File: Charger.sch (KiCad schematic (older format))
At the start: 2 parts

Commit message: added ckt
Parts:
- removed R? (x2): R, symbol Device:R
- added C? (x3): CAP, symbol pspice:CAP
- added D? (x4): 1N914, Diode_THT:D_DO-35_SOD27_P7.62mm_Horizontal, symbol Diode:1N914
- added D?: BZX84Cxx, Diode_SMD:D_SOT-23_ANK, symbol Diode:BZX84Cxx
- added R? (x2): R, symbol Device:R
- added U?: LT1085-5.0, symbol Regulator_Linear:LT1085-5.0
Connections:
- net labels added: AC, GND
- wire segments 0 -> 35
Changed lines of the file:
@@
 $EndDescr
 $Comp
+L Diode:1N914 D?
+U 1 1 6031057C
+P 3100 2550
+F 0 "D?" V 3054 2630 50  0000 L CNN
+F 1 "1N914" V 3145 2630 50  0000 L CNN
+F 2 "Diode_THT:D_DO-35_SOD27_P7.62mm_Horizontal" H 3100 2375 50  0001 C CNN
+F 3 "http://www.vishay.com/docs/85622/1n914.pdf" H 3100 2550 50  0001 C CNN
+	1    3100 2550
+	0    1    1    0
+$EndComp
+$Comp
+L Diode:1N914 D?
+U 1 1 60311C82
+P 3100 3800
+F 0 "D?" V 3054 3880 50  0000 L CNN
+F 1 "1N914" V 3145 3880 50  0000 L CNN
+F 2 "Diode_THT:D_DO-35_SOD27_P7.62mm_Horizontal" H 3100 3625 50  0001 C CNN
+F 3 "http://www.vishay.com/docs/85622/1n914.pdf" H 3100 3800 50  0001 C CNN
+	1    3100 3800
+	0    1    1    0
+$EndComp
+$Comp
+L Diode:1N914 D?
+U 1 1 60312AAD
+P 4200 2550
+F 0 "D?" V 4154 2630 50  0000 L CNN
+F 1 "1N914" V 4245 2630 50  0000 L CNN
+F 2 "Diode_THT:D_DO-35_SOD27_P7.62mm_Horizontal" H 4200 2375 50  0001 C CNN
+F 3 "http://www.vishay.com/docs/85622/1n914.pdf" H 4200 2550 50  0001 C CNN
+	1    4200 2550
+	0    1    1    0
+$EndComp
+$Comp
+L Diode:1N914 D?
+U 1 1 60313CDB
+P 4200 3800
+F 0 "D?" V 4154 3880 50  0000 L CNN
+F 1 "1N914" V 4245 3880 50  0000 L CNN
+F 2 "Diode_THT:D_DO-35_SOD27_P7.62mm_Horizontal" H 4200 3625 50  0001 C CNN
+F 3 "http://www.vishay.com/docs/85622/1n914.pdf" H 4200 3800 50  0001 C CNN
+	1    4200 3800
+	0    1    1    0
+$EndComp
+$Comp
+L pspice:CAP C?
+U 1 1 60316869
+P 5050 3250
+F 0 "C?" H 5228 3296 50  0000 L CNN
+F 1 "CAP" H 5228 3205 50  0000 L CNN
+F 2 "" H 5050 3250 50  0001 C CNN
+F 3 "~" H 5050 3250 50  0001 C CNN
+	1    5050 3250
+	1    0    0    -1
+$EndComp
+$Comp
+L Diode:BZX84Cxx D?
+U 1 1 603170B0
+P 6000 3550
+F 0 "D?" V 5954 3630 50  0000 L CNN
+F 1 "BZX84Cxx" V 6045 3630 50  0000 L CNN
+F 2 "Diode_SMD:D_SOT-23_ANK" H 6000 3375 50  0001 C CNN
+F 3 "https://diotec.com/tl_files/diotec/files/pdf/datasheets/bzx84c2v4.pdf" H 6000 3550 50  0001 C CNN
+	1    6000 3550
+	0    1    1    0
+$EndComp
+$Comp
 L Device:R R?
-U 1 1 60309E92
-P 5400 2800
-F 0 "R?" H 5470 2846 50  0000 L CNN
-F 1 "R" H 5470 2755 50  0000 L CNN
-F 2 "" V 5330 2800 50  0001 C CNN
-F 3 "~" H 5400 2800 50  0001 C CNN
-	1    5400 2800
+U 1 1 60317AB7
+P 6000 2550
+F 0 "R?" H 6070 2596 50  0000 L CNN
+F 1 "R" H 6070 2505 50  0000 L CNN
+F 2 "" V 5930 2550 50  0001 C CNN
+F 3 "~" H 6000 2550 50  0001 C CNN
+	1    6000 2550
+	1    0    0    -1
+$EndComp
+$Comp
+L pspice:CAP C?
+U 1 1 60318512
+P 7000 2950
+F 0 "C?" H 7178 2996 50  0000 L CNN
+F 1 "CAP" H 7178 2905 50  0000 L CNN
+F 2 "" H 7000 2950 50  0001 C CNN
+F 3 "~" H 7000 2950 50  0001 C CNN
+	1    7000 2950
+	1    0    0    -1
+$EndComp
+$Comp
+L pspice:CAP C?
+U 1 1 6031AA99
+P 9650 3100
+F 0 "C?" H 9828 3146 50  0000 L CNN
+F 1 "CAP" H 9828 3055 50  0000 L CNN
+F 2 "" H 9650 3100 50  0001 C CNN
+F 3 "~" H 9650 3100 50  0001 C CNN
+	1    9650 3100
 	1    0    0    -1
 $EndComp
 $Comp
 L Device:R R?
-U 1 1 6030A5AE
-P 4450 2850
-F 0 "R?" H 4520 2896 50  0000 L CNN
-F 1 "R" H 4520 2805 50  0000 L CNN
-F 2 "" V 4380 2850 50  0001 C CNN
-F 3 "~" H 4450 2850 50  0001 C CNN
-	1    4450 2850
-	1    0    0    -1
-$EndComp
+U 1 1 6031AFD1
+P 10350 3100
+F 0 "R?" H 10420 3146 50  0000 L CNN
+F 1 "R" H 10420 3055 50  0000 L CNN
+F 2 "" V 10280 3100 50  0001 C CNN
+F 3 "~" H 10350 3100 50  0001 C CNN
+	1    10350 3100
+	1    0    0    -1
+$EndComp
+$Comp
+L Regulator_Linear:LT1085-5.0 U?
+U 1 1 6031B799
+P 8100 2200
+F 0 "U?" H 8100 2442 50  0000 C CNN
+F 1 "LT1085-5.0" H 8100 2351 50  0000 C CNN
+F 2 "" H 8100 2450 50  0001 C CIN
+F 3 "https://www.analog.com/media/en/technical-documentation/data-sheets/1083ffe.pdf" H 8100 2200 50  0001 C CNN
+	1    8100 2200
+	1    0    0    -1
+$EndComp
+Wire Wire Line
+	8450 2200 9650 2200
+Wire Wire Line
+	3100 3950 3100 4150
+Wire Wire Line
+	3100 4150 4200 4150
+Wire Wire Line
+	4200 4150 4200 3950
+Wire Wire Line
+	4200 3650 4200 2700
+Wire Wire Line
+	4200 2400 4200 2200
+Wire Wire Line
+	4200 2200 3100 2200
+Wire Wire Line
+	3100 2200 3100 2400
+Wire Wire Line
+	3100 2700 3100 3650
+Wire Wire Line
+	5050 3000 5050 2200
+Wire Wire Line
+	5050 2200 4200 2200
+Connection ~ 4200 2200
+Wire Wire Line
+	5050 3500 5050 4150
+Wire Wire Line
+	5050 4150 4200 4150
+Connection ~ 4200 4150
+Wire Wire Line
+	6000 4150 6000 3700
+Wire Wire Line
+	6000 3400 6000 3000
+Wire Wire Line
+	6000 2400 6000 2200
+Wire Wire Line
+	6000 2200 5050 2200
+Connection ~ 5050 2200
+Wire Wire Line
+	6000 3000 6500 3000
+Wire Wire Line
+	6500 3000 6500 2200
+Wire Wire Line
+	6500 2200 7000 2200
+Wire Wire Line
+	7000 2200 7000 2700
+Connection ~ 6000 3000
+Wire Wire Line
+	6000 3000 6000 2700
+Wire Wire Line
+	7000 3200 7000 4150
+Wire Wire Line
+	7000 4150 6000 4150
+Connection ~ 6000 4150
+Wire Wire Line
+	5050 4150 6000 4150
+Connection ~ 5050 4150
+Wire Wire Line
+	7000 2200 7800 2200
+Connection ~ 7000 2200
+Wire Wire Line
+	7000 4150 8100 4150
+Wire Wire Line
+	10350 4150 10350 3250
+Connection ~ 7000 4150
+Connection ~ 9650 4150
+Wire Wire Line
+	9650 4150 10350 4150
+Connection ~ 9650 2200
+Wire Wire Line
+	9650 2200 10350 2200
+Wire Wire Line
+	9650 3350 9650 4150
+Wire Wire Line
+	9650 2200 9650 2850
+Wire Wire Line
+	10350 2200 10350 2950
+Wire Wire Line
+	8100 2500 8100 4150
+Connection ~ 8100 4150
+Wire Wire Line
+	8100 4150 9650 4150
+$Comp
+L power:GND #PWR?
+U 1 1 6032C60B
+P 7000 4150
+F 0 "#PWR?" H 7000 3900 50  0001 C CNN
+F 1 "GND" H 7005 3977 50  0000 C CNN
+F 2 "" H 7000 4150 50  0001 C CNN
+F 3 "" H 7000 4150 50  0001 C CNN
+	1    7000 4150
+	1    0    0    -1
+$EndComp
+$Comp
+L power:AC #PWR?
+U 1 1 6032CF48
+P 1500 3100
+F 0 "#PWR?" H 1500 3000 50  0001 C CNN
+F 1 "AC" H 1500 3375 50  0000 C CNN
+F 2 "" H 1500 3100 50  0001 C CNN
+F 3 "" H 1500 3100 50  0001 C CNN
+	1    1500 3100
+	1    0    0    -1
+$EndComp

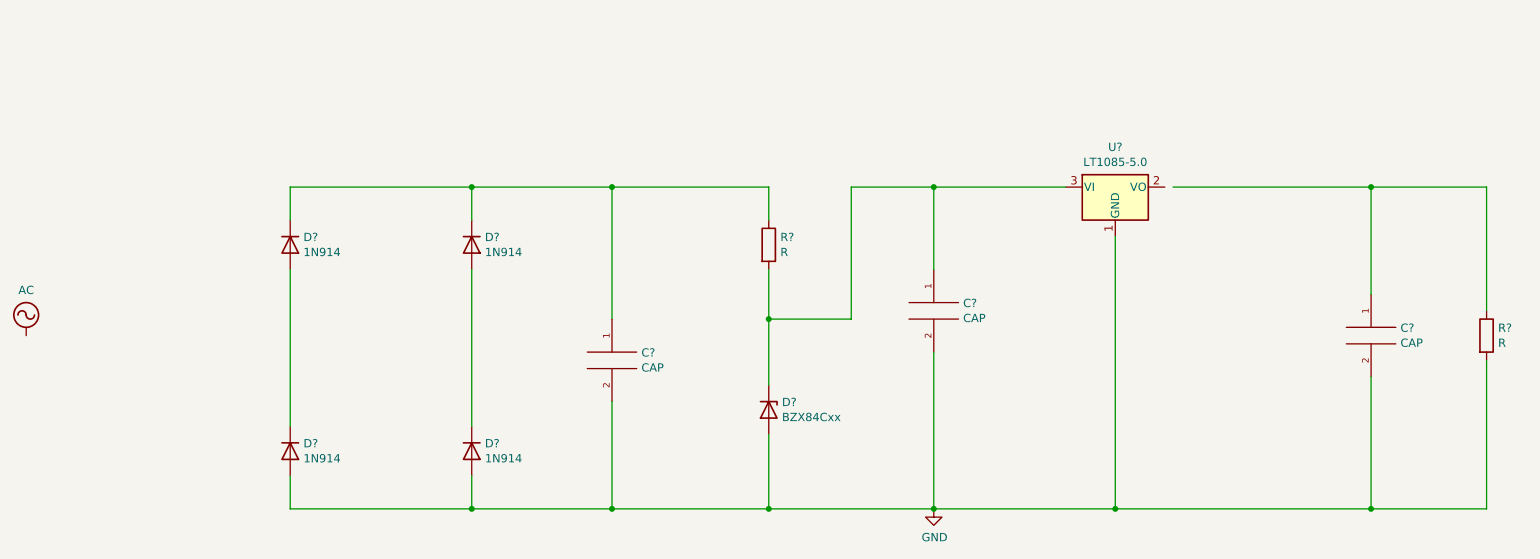
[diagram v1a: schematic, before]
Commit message: schematics updated
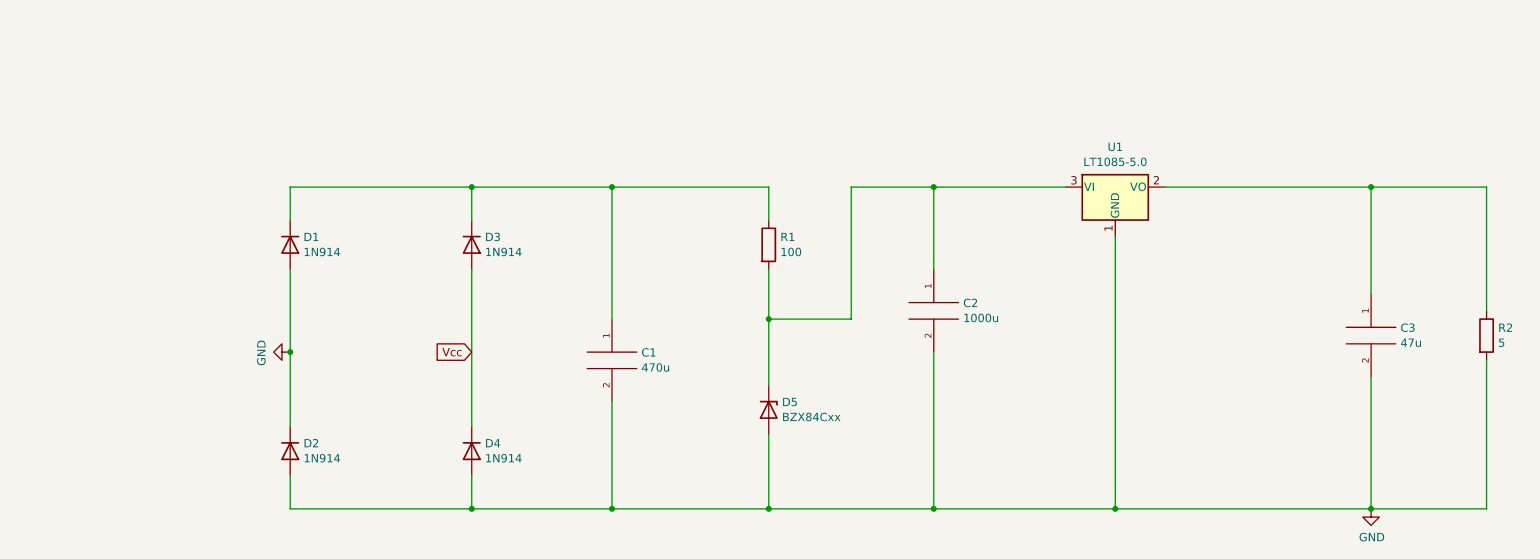
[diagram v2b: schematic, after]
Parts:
- C1: renamed from C?; value CAP -> 470u; footprint (none) -> Capacitor_SMD:CP_Elec_3x5.3
- C2: renamed from C?; value CAP -> 1000u; footprint (none) -> Capacitor_SMD:CP_Elec_3x5.3
- C3: renamed from C?; value CAP -> 47u; footprint (none) -> Capacitor_SMD:CP_Elec_3x5.3
- D1, D2, D3, D4: renamed from D?; footprint Diode_THT:D_DO-35_SOD27_P7.62mm_Horizontal -> Diode_SMD:D_0201_0603Metric
- R1: renamed from R?; value R -> 100; footprint (none) -> Resistor_SMD:R_0201_0603Metric
- R2: renamed from R?; value R -> 5; footprint (none) -> Resistor_SMD:R_0201_0603Metric
- gave numbers to parts that had none: 2
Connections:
- net labels added: Vcc
- net labels removed: AC
- wire segments 35 -> 36
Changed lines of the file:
@@
 $EndDescr
 $Comp
-L Diode:1N914 D?
+L Diode:1N914 D1
 U 1 1 6031057C
 P 3100 2550
-F 0 "D?" V 3054 2630 50  0000 L CNN
+F 0 "D1" V 3054 2630 50  0000 L CNN
 F 1 "1N914" V 3145 2630 50  0000 L CNN
-F 2 "Diode_THT:D_DO-35_SOD27_P7.62mm_Horizontal" H 3100 2375 50  0001 C CNN
+F 2 "Diode_SMD:D_0201_0603Metric" H 3100 2375 50  0001 C CNN
 F 3 "http://www.vishay.com/docs/85622/1n914.pdf" H 3100 2550 50  0001 C CNN
 	1    3100 2550
@@
 $EndComp
 $Comp
-L Diode:1N914 D?
+L Diode:1N914 D2
 U 1 1 60311C82
 P 3100 3800
-F 0 "D?" V 3054 3880 50  0000 L CNN
+F 0 "D2" V 3054 3880 50  0000 L CNN
 F 1 "1N914" V 3145 3880 50  0000 L CNN
-F 2 "Diode_THT:D_DO-35_SOD27_P7.62mm_Horizontal" H 3100 3625 50  0001 C CNN
+F 2 "Diode_SMD:D_0201_0603Metric" H 3100 3625 50  0001 C CNN
 F 3 "http://www.vishay.com/docs/85622/1n914.pdf" H 3100 3800 50  0001 C CNN
 	1    3100 3800
@@
 $EndComp
 $Comp
-L Diode:1N914 D?
+L Diode:1N914 D3
 U 1 1 60312AAD
 P 4200 2550
-F 0 "D?" V 4154 2630 50  0000 L CNN
+F 0 "D3" V 4154 2630 50  0000 L CNN
 F 1 "1N914" V 4245 2630 50  0000 L CNN
-F 2 "Diode_THT:D_DO-35_SOD27_P7.62mm_Horizontal" H 4200 2375 50  0001 C CNN
+F 2 "Diode_SMD:D_0201_0603Metric" H 4200 2375 50  0001 C CNN
 F 3 "http://www.vishay.com/docs/85622/1n914.pdf" H 4200 2550 50  0001 C CNN
 	1    4200 2550
@@
 $EndComp
 $Comp
-L Diode:1N914 D?
+L Diode:1N914 D4
 U 1 1 60313CDB
 P 4200 3800
-F 0 "D?" V 4154 3880 50  0000 L CNN
+F 0 "D4" V 4154 3880 50  0000 L CNN
 F 1 "1N914" V 4245 3880 50  0000 L CNN
-F 2 "Diode_THT:D_DO-35_SOD27_P7.62mm_Horizontal" H 4200 3625 50  0001 C CNN
+F 2 "Diode_SMD:D_0201_0603Metric" H 4200 3625 50  0001 C CNN
 F 3 "http://www.vishay.com/docs/85622/1n914.pdf" H 4200 3800 50  0001 C CNN
 	1    4200 3800
@@
 $EndComp
 $Comp
-L pspice:CAP C?
+L pspice:CAP C1
 U 1 1 60316869
 P 5050 3250
-F 0 "C?" H 5228 3296 50  0000 L CNN
-F 1 "CAP" H 5228 3205 50  0000 L CNN
-F 2 "" H 5050 3250 50  0001 C CNN
+F 0 "C1" H 5228 3296 50  0000 L CNN
+F 1 "470u" H 5228 3205 50  0000 L CNN
+F 2 "Capacitor_SMD:CP_Elec_3x5.3" H 5050 3250 50  0001 C CNN
 F 3 "~" H 5050 3250 50  0001 C CNN
 	1    5050 3250
@@
 $EndComp
 $Comp
-L Diode:BZX84Cxx D?
+L Diode:BZX84Cxx D5
 U 1 1 603170B0
 P 6000 3550
-F 0 "D?" V 5954 3630 50  0000 L CNN
+F 0 "D5" V 5954 3630 50  0000 L CNN
 F 1 "BZX84Cxx" V 6045 3630 50  0000 L CNN
 F 2 "Diode_SMD:D_SOT-23_ANK" H 6000 3375 50  0001 C CNN
@@
 $EndComp
 $Comp
-L Device:R R?
+L Device:R R1
 U 1 1 60317AB7
 P 6000 2550
-F 0 "R?" H 6070 2596 50  0000 L CNN
-F 1 "R" H 6070 2505 50  0000 L CNN
-F 2 "" V 5930 2550 50  0001 C CNN
+F 0 "R1" H 6070 2596 50  0000 L CNN
+F 1 "100" H 6070 2505 50  0000 L CNN
+F 2 "Resistor_SMD:R_0201_0603Metric" V 5930 2550 50  0001 C CNN
 F 3 "~" H 6000 2550 50  0001 C CNN
 	1    6000 2550
@@
 $EndComp
 $Comp
-L pspice:CAP C?
+L pspice:CAP C2
 U 1 1 60318512
 P 7000 2950
-F 0 "C?" H 7178 2996 50  0000 L CNN
-F 1 "CAP" H 7178 2905 50  0000 L CNN
-F 2 "" H 7000 2950 50  0001 C CNN
+F 0 "C2" H 7178 2996 50  0000 L CNN
+F 1 "1000u" H 7178 2905 50  0000 L CNN
+F 2 "Capacitor_SMD:CP_Elec_3x5.3" H 7000 2950 50  0001 C CNN
 F 3 "~" H 7000 2950 50  0001 C CNN
 	1    7000 2950
@@
 $EndComp
 $Comp
-L pspice:CAP C?
-U 1 1 6031AA99
-P 9650 3100
-F 0 "C?" H 9828 3146 50  0000 L CNN
-F 1 "CAP" H 9828 3055 50  0000 L CNN
-F 2 "" H 9650 3100 50  0001 C CNN
-F 3 "~" H 9650 3100 50  0001 C CNN
-	1    9650 3100
-	1    0    0    -1
-$EndComp
-$Comp
-L Device:R R?
+L Device:R R2
 U 1 1 6031AFD1
 P 10350 3100
-F 0 "R?" H 10420 3146 50  0000 L CNN
-F 1 "R" H 10420 3055 50  0000 L CNN
-F 2 "" V 10280 3100 50  0001 C CNN
+F 0 "R2" H 10420 3146 50  0000 L CNN
+F 1 "5" H 10420 3055 50  0000 L CNN
+F 2 "Resistor_SMD:R_0201_0603Metric" V 10280 3100 50  0001 C CNN
 F 3 "~" H 10350 3100 50  0001 C CNN
 	1    10350 3100
@@
 $EndComp
 $Comp
-L Regulator_Linear:LT1085-5.0 U?
+L Regulator_Linear:LT1085-5.0 U1
 U 1 1 6031B799
 P 8100 2200
-F 0 "U?" H 8100 2442 50  0000 C CNN
+F 0 "U1" H 8100 2442 50  0000 C CNN
 F 1 "LT1085-5.0" H 8100 2351 50  0000 C CNN
 F 2 "" H 8100 2450 50  0001 C CIN
@@
 $EndComp
 Wire Wire Line
-	8450 2200 9650 2200
-Wire Wire Line
 	3100 3950 3100 4150
 Wire Wire Line
@@
 	3100 2200 3100 2400
 Wire Wire Line
-	3100 2700 3100 3650
+	3100 2700 3100 3200
 Wire Wire Line
 	5050 3000 5050 2200
@@
 	8100 4150 9650 4150
 $Comp
-L power:GND #PWR?
+L power:GND #PWR01
 U 1 1 6032C60B
-P 7000 4150
-F 0 "#PWR?" H 7000 3900 50  0001 C CNN
-F 1 "GND" H 7005 3977 50  0000 C CNN
-F 2 "" H 7000 4150 50  0001 C CNN
-F 3 "" H 7000 4150 50  0001 C CNN
-	1    7000 4150
-	1    0    0    -1
-$EndComp
-$Comp
-L power:AC #PWR?
-U 1 1 6032CF48
-P 1500 3100
-F 0 "#PWR?" H 1500 3000 50  0001 C CNN
-F 1 "AC" H 1500 3375 50  0000 C CNN
-F 2 "" H 1500 3100 50  0001 C CNN
-F 3 "" H 1500 3100 50  0001 C CNN
-	1    1500 3100
-	1    0    0    -1
-$EndComp
+P 3100 3200
+F 0 "#PWR01" H 3100 2950 50  0001 C CNN
+F 1 "GND" H 3105 3027 50  0000 C CNN
+F 2 "" H 3100 3200 50  0001 C CNN
+F 3 "" H 3100 3200 50  0001 C CNN
+	1    3100 3200
+	0    1    1    0
+$EndComp
+Text GLabel 4200 3200 0    50   Input ~ 0
+Vcc
+Connection ~ 3100 3200
+Wire Wire Line
+	3100 3200 3100 3650
+$Comp
+L pspice:CAP C3
+U 1 1 6031AA99
+P 9650 3100
+F 0 "C3" H 9828 3146 50  0000 L CNN
+F 1 "47u" H 9828 3055 50  0000 L CNN
+F 2 "Capacitor_SMD:CP_Elec_3x5.3" H 9650 3100 50  0001 C CNN
+F 3 "~" H 9650 3100 50  0001 C CNN
+	1    9650 3100
+	1    0    0    -1
+$EndComp
+Wire Wire Line
+	8400 2200 9650 2200
+$Comp
+L power:GND #PWR0101
+U 1 1 60314248
+P 9650 4150
+F 0 "#PWR0101" H 9650 3900 50  0001 C CNN
+F 1 "GND" H 9655 3977 50  0000 C CNN
+F 2 "" H 9650 4150 50  0001 C CNN
+F 3 "" H 9650 4150 50  0001 C CNN
+	1    9650 4150
+	1    0    0    -1
+$EndComp

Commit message: pcb designed
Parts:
- U1: footprint (none) -> LT1085_charger:TO220L1
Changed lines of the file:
@@
 F 0 "U1" H 8100 2442 50  0000 C CNN
 F 1 "LT1085-5.0" H 8100 2351 50  0000 C CNN
-F 2 "" H 8100 2450 50  0001 C CIN
+F 2 "LT1085_charger:TO220L1" H 8100 2450 50  0001 C CIN
 F 3 "https://www.analog.com/media/en/technical-documentation/data-sheets/1083ffe.pdf" H 8100 2200 50  0001 C CNN
 	1    8100 2200

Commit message: major changes
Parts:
- removed D1, D2, D3, D4: 1N914, Diode_SMD:D_0201_0603Metric, symbol Diode:1N914
- added D1, D2, D3, D4: 1N4005, Diode_THT:D_DO-41_SOD81_P10.16mm_Horizontal, symbol Diode:1N4005
- added J1: Input, symbol Connector:Screw_Terminal_01x02
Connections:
- net GND: now also D1.2 (A), D2.1 (K), D2.2 (A), D4.2 (A), J1.2 (Pin_2)
- net Vcc: now also D3.2 (A), D4.1 (K), J1.1 (Pin_1)
- net at C1.1, R1.1: now also D1.1 (K), D3.1 (K)
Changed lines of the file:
@@
 encoding utf-8
 Sheet 1 1
-Title ""
+Title "Charger"
 Date ""
 Rev ""
@@
 Comment1 ""
 Comment2 ""
-Comment3 ""
-Comment4 ""
+Comment3 "For ELP305 Lab"
+Comment4 "Author : Bhoopendra Uikey"
 $EndDescr
-$Comp
-L Diode:1N914 D1
-U 1 1 6031057C
-P 3100 2550
-F 0 "D1" V 3054 2630 50  0000 L CNN
-F 1 "1N914" V 3145 2630 50  0000 L CNN
-F 2 "Diode_SMD:D_0201_0603Metric" H 3100 2375 50  0001 C CNN
-F 3 "http://www.vishay.com/docs/85622/1n914.pdf" H 3100 2550 50  0001 C CNN
-	1    3100 2550
-	0    1    1    0
-$EndComp
-$Comp
-L Diode:1N914 D2
-U 1 1 60311C82
-P 3100 3800
-F 0 "D2" V 3054 3880 50  0000 L CNN
-F 1 "1N914" V 3145 3880 50  0000 L CNN
-F 2 "Diode_SMD:D_0201_0603Metric" H 3100 3625 50  0001 C CNN
-F 3 "http://www.vishay.com/docs/85622/1n914.pdf" H 3100 3800 50  0001 C CNN
-	1    3100 3800
-	0    1    1    0
-$EndComp
-$Comp
-L Diode:1N914 D3
-U 1 1 60312AAD
-P 4200 2550
-F 0 "D3" V 4154 2630 50  0000 L CNN
-F 1 "1N914" V 4245 2630 50  0000 L CNN
-F 2 "Diode_SMD:D_0201_0603Metric" H 4200 2375 50  0001 C CNN
-F 3 "http://www.vishay.com/docs/85622/1n914.pdf" H 4200 2550 50  0001 C CNN
-	1    4200 2550
-	0    1    1    0
-$EndComp
-$Comp
-L Diode:1N914 D4
-U 1 1 60313CDB
-P 4200 3800
-F 0 "D4" V 4154 3880 50  0000 L CNN
-F 1 "1N914" V 4245 3880 50  0000 L CNN
-F 2 "Diode_SMD:D_0201_0603Metric" H 4200 3625 50  0001 C CNN
-F 3 "http://www.vishay.com/docs/85622/1n914.pdf" H 4200 3800 50  0001 C CNN
-	1    4200 3800
-	0    1    1    0
-$EndComp
 $Comp
 L pspice:CAP C1
@@
 	1    0    0    -1
 $EndComp
+$Comp
+L Connector:Screw_Terminal_01x02 J1
+U 1 1 6031590C
+P 2150 3100
+F 0 "J1" H 2230 3092 50  0000 L CNN
+F 1 "Input" H 2230 3001 50  0000 L CNN
+F 2 "" H 2150 3100 50  0001 C CNN
+F 3 "~" H 2150 3100 50  0001 C CNN
+	1    2150 3100
+	1    0    0    -1
+$EndComp
+Text GLabel 1950 3100 0    50   Input ~ 0
+Vcc
+$Comp
+L power:GND #PWR02
+U 1 1 6031992D
+P 1950 3200
+F 0 "#PWR02" H 1950 2950 50  0001 C CNN
+F 1 "GND" H 1955 3027 50  0000 C CNN
+F 2 "" H 1950 3200 50  0001 C CNN
+F 3 "" H 1950 3200 50  0001 C CNN
+	1    1950 3200
+	1    0    0    -1
+$EndComp
+$Comp
+L Diode:1N4005 D3
+U 1 1 60321173
+P 4200 2550
+F 0 "D3" V 4154 2630 50  0000 L CNN
+F 1 "1N4005" V 4245 2630 50  0000 L CNN
+F 2 "Diode_THT:D_DO-41_SOD81_P10.16mm_Horizontal" H 4200 2375 50  0001 C CNN
+F 3 "http://www.vishay.com/docs/88503/1n4001.pdf" H 4200 2550 50  0001 C CNN
+	1    4200 2550
+	0    1    1    0
+$EndComp
+$Comp
+L Diode:1N4005 D1
+U 1 1 60321C5D
+P 3100 2550
+F 0 "D1" V 3054 2630 50  0000 L CNN
+F 1 "1N4005" V 3145 2630 50  0000 L CNN
+F 2 "Diode_THT:D_DO-41_SOD81_P10.16mm_Horizontal" H 3100 2375 50  0001 C CNN
+F 3 "http://www.vishay.com/docs/88503/1n4001.pdf" H 3100 2550 50  0001 C CNN
+	1    3100 2550
+	0    1    1    0
+$EndComp
+$Comp
+L Diode:1N4005 D2
+U 1 1 603225FE
+P 3100 3800
+F 0 "D2" V 3054 3880 50  0000 L CNN
+F 1 "1N4005" V 3145 3880 50  0000 L CNN
+F 2 "Diode_THT:D_DO-41_SOD81_P10.16mm_Horizontal" H 3100 3625 50  0001 C CNN
+F 3 "http://www.vishay.com/docs/88503/1n4001.pdf" H 3100 3800 50  0001 C CNN
+	1    3100 3800
+	0    1    1    0
+$EndComp
+$Comp
+L Diode:1N4005 D4
+U 1 1 60322E34
+P 4200 3800
+F 0 "D4" V 4154 3880 50  0000 L CNN
+F 1 "1N4005" V 4245 3880 50  0000 L CNN
+F 2 "Diode_THT:D_DO-41_SOD81_P10.16mm_Horizontal" H 4200 3625 50  0001 C CNN
+F 3 "http://www.vishay.com/docs/88503/1n4001.pdf" H 4200 3800 50  0001 C CNN
+	1    4200 3800
+	0    1    1    0
+$EndComp
 $EndSCHEMATC
